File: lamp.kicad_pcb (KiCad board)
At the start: 2 copper layers, 74.7 x 38.6 mm, 25 parts, among them J1 Screw_Terminal_01x02, J2 Screw_Terminal_01x02, J3 Conn_01x04_Pin, K1 G3MB202PDC12, Q1 BC547, U1 ESP-12E, U3 AMS1117-3.3

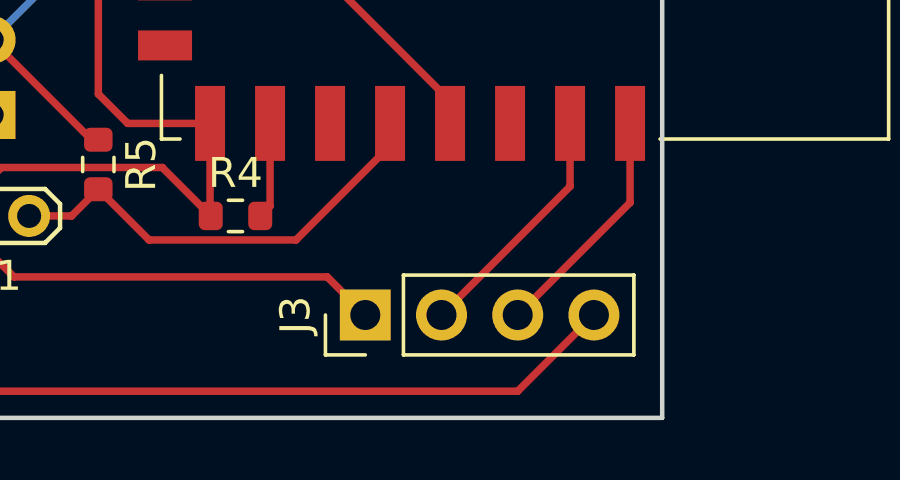
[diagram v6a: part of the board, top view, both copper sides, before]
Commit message: fix jumper side
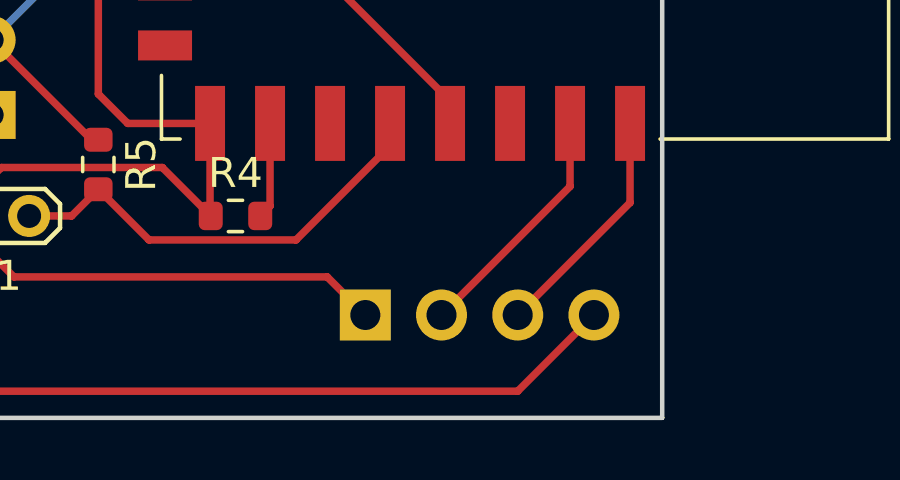
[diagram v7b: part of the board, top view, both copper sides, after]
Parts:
- J3: moved to B.Cu
- turned J3 to -90 degrees
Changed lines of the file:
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@@
-    )
-  )
-  (footprint "Connector_PinHeader_2.54mm:PinHeader_1x04_P2.54mm_Vertical" (layer "F.Cu")
-    (at 179.08 133.35 90)
-    (descr "Through hole straight pin header, 1x04, 2.54mm pitch, single row")
-    (tags "Through hole pin header THT 1x04 2.54mm single row")
-    (property "Sheetfile" "lamp.kicad_sch")
-    (property "Sheetname" "")
-    (property "ki_description" "Generic connector, single row, 01x04, script generated")
-    (property "ki_keywords" "connector")
-    (attr through_hole)
-    (fp_text reference "J3" (at 0 -2.33 90) (layer "F.SilkS")
-        (effects (font (size 1 1) (thickness 0.15)))
-    )
-    (fp_text value "Conn_01x04_Pin" (at 0 9.95 90) (layer "F.Fab") hide
-        (effects (font (size 1 1) (thickness 0.15)))
-    )
-    (fp_text user "${REFERENCE}" (at 0 3.81) (layer "F.Fab")
-        (effects (font (size 1 1) (thickness 0.15)))
-    )
-    (fp_line (start -1.33 -1.33) (end 0 -1.33)
-      (stroke (width 0.12) (type solid)) (layer "F.SilkS"))
-    (fp_line (start -1.33 0) (end -1.33 -1.33)
-      (stroke (width 0.12) (type solid)) (layer "F.SilkS"))
-    (fp_line (start -1.33 1.27) (end -1.33 8.95)
-      (stroke (width 0.12) (type solid)) (layer "F.SilkS"))
-    (fp_line (start -1.33 1.27) (end 1.33 1.27)
-      (stroke (width 0.12) (type solid)) (layer "F.SilkS"))
-    (fp_line (start -1.33 8.95) (end 1.33 8.95)
-      (stroke (width 0.12) (type solid)) (layer "F.SilkS"))
-    (fp_line (start 1.33 1.27) (end 1.33 8.95)
-      (stroke (width 0.12) (type solid)) (layer "F.SilkS"))
-    (fp_line (start -1.8 -1.8) (end -1.8 9.4)
-      (stroke (width 0.05) (type solid)) (layer "F.CrtYd"))
-    (fp_line (start -1.8 9.4) (end 1.8 9.4)
-      (stroke (width 0.05) (type solid)) (layer "F.CrtYd"))
-    (fp_line (start 1.8 -1.8) (end -1.8 -1.8)
-      (stroke (width 0.05) (type solid)) (layer "F.CrtYd"))
-    (fp_line (start 1.8 9.4) (end 1.8 -1.8)
-      (stroke (width 0.05) (type solid)) (layer "F.CrtYd"))
-    (fp_line (start -1.27 -0.635) (end -0.635 -1.27)
-      (stroke (width 0.1) (type solid)) (layer "F.Fab"))
-    (fp_line (start -1.27 8.89) (end -1.27 -0.635)
-      (stroke (width 0.1) (type solid)) (layer "F.Fab"))
-    (fp_line (start -0.635 -1.27) (end 1.27 -1.27)
-      (stroke (width 0.1) (type solid)) (layer "F.Fab"))
-    (fp_line (start 1.27 -1.27) (end 1.27 8.89)
-      (stroke (width 0.1) (type solid)) (layer "F.Fab"))
-    (fp_line (start 1.27 8.89) (end -1.27 8.89)
-      (stroke (width 0.1) (type solid)) (layer "F.Fab"))
-    (pad "1" thru_hole rect (at 0 0 90) (size 1.7 1.7) (drill 1) (layers "*.Cu" "*.Mask")
-      (net 1 "GND") (pinfunction "Pin_1") (pintype "passive"))
-    (pad "2" thru_hole oval (at 0 2.54 90) (size 1.7 1.7) (drill 1) (layers "*.Cu" "*.Mask")
-      (net 29 "Net-(J3-Pin_2)") (pinfunction "Pin_2") (pintype "passive"))
-    (pad "3" thru_hole oval (at 0 5.08 90) (size 1.7 1.7) (drill 1) (layers "*.Cu" "*.Mask")
-      (net 30 "Net-(J3-Pin_3)") (pinfunction "Pin_3") (pintype "passive"))
-    (pad "4" thru_hole oval (at 0 7.62 90) (size 1.7 1.7) (drill 1) (layers "*.Cu" "*.Mask")
-      (net 31 "Net-(J3-Pin_4)") (pinfunction "Pin_4") (pintype "passive"))
-    (model "${KICAD6_3DMODEL_DIR}/Connector_PinHeader_2.54mm.3dshapes/PinHeader_1x04_P2.54mm_Vertical.wrl"
-      (offset (xyz 0 0 0))
-      (scale (xyz 1 1 1))
-      (rotate (xyz 0 0 0))
     )
   )
@@
       (net 3 "Net-(D1-K)") (pinfunction "-") (pintype "power_in"))
   )
+  (footprint "Connector_PinHeader_2.54mm:PinHeader_1x04_P2.54mm_Vertical" (layer "B.Cu")
+    (at 179.08 133.35 -90)
+    (descr "Through hole straight pin header, 1x04, 2.54mm pitch, single row")
+    (tags "Through hole pin header THT 1x04 2.54mm single row")
+    (property "Sheetfile" "lamp.kicad_sch")
+    (property "Sheetname" "")
+    (property "ki_description" "Generic connector, single row, 01x04, script generated")
+    (property "ki_keywords" "connector")
+    (attr through_hole)
+    (fp_text reference "J3" (at 0 2.33 90) (layer "B.SilkS")
+        (effects (font (size 1 1) (thickness 0.15)) (justify mirror))
+    )
+    (fp_text value "Conn_01x04_Pin" (at 0 -9.95 90) (layer "B.Fab") hide
+        (effects (font (size 1 1) (thickness 0.15)) (justify mirror))
+    )
+    (fp_text user "${REFERENCE}" (at 0 -3.81) (layer "B.Fab")
+        (effects (font (size 1 1) (thickness 0.15)) (justify mirror))
+    )
+    (fp_line (start -1.33 -8.95) (end 1.33 -8.95)
+      (stroke (width 0.12) (type solid)) (layer "B.SilkS"))
+    (fp_line (start -1.33 -1.27) (end -1.33 -8.95)
+      (stroke (width 0.12) (type solid)) (layer "B.SilkS"))
+    (fp_line (start -1.33 -1.27) (end 1.33 -1.27)
+      (stroke (width 0.12) (type solid)) (layer "B.SilkS"))
+    (fp_line (start -1.33 0) (end -1.33 1.33)
+      (stroke (width 0.12) (type solid)) (layer "B.SilkS"))
+    (fp_line (start -1.33 1.33) (end 0 1.33)
+      (stroke (width 0.12) (type solid)) (layer "B.SilkS"))
+    (fp_line (start 1.33 -1.27) (end 1.33 -8.95)
+      (stroke (width 0.12) (type solid)) (layer "B.SilkS"))
+    (fp_line (start -1.8 -9.4) (end 1.8 -9.4)
+      (stroke (width 0.05) (type solid)) (layer "B.CrtYd"))
+    (fp_line (start -1.8 1.8) (end -1.8 -9.4)
+      (stroke (width 0.05) (type solid)) (layer "B.CrtYd"))
+    (fp_line (start 1.8 -9.4) (end 1.8 1.8)
+      (stroke (width 0.05) (type solid)) (layer "B.CrtYd"))
+    (fp_line (start 1.8 1.8) (end -1.8 1.8)
+      (stroke (width 0.05) (type solid)) (layer "B.CrtYd"))
+    (fp_line (start -1.27 -8.89) (end -1.27 0.635)
+      (stroke (width 0.1) (type solid)) (layer "B.Fab"))
+    (fp_line (start -1.27 0.635) (end -0.635 1.27)
+      (stroke (width 0.1) (type solid)) (layer "B.Fab"))
+    (fp_line (start -0.635 1.27) (end 1.27 1.27)
+      (stroke (width 0.1) (type solid)) (layer "B.Fab"))
+    (fp_line (start 1.27 -8.89) (end -1.27 -8.89)
+      (stroke (width 0.1) (type solid)) (layer "B.Fab"))
+    (fp_line (start 1.27 1.27) (end 1.27 -8.89)
+      (stroke (width 0.1) (type solid)) (layer "B.Fab"))
+    (pad "1" thru_hole rect (at 0 0 270) (size 1.7 1.7) (drill 1) (layers "*.Cu" "*.Mask")
+      (net 1 "GND") (pinfunction "Pin_1") (pintype "passive"))
+    (pad "2" thru_hole oval (at 0 -2.54 270) (size 1.7 1.7) (drill 1) (layers "*.Cu" "*.Mask")
+      (net 29 "Net-(J3-Pin_2)") (pinfunction "Pin_2") (pintype "passive"))
+    (pad "3" thru_hole oval (at 0 -5.08 270) (size 1.7 1.7) (drill 1) (layers "*.Cu" "*.Mask")
+      (net 30 "Net-(J3-Pin_3)") (pinfunction "Pin_3") (pintype "passive"))
+    (pad "4" thru_hole oval (at 0 -7.62 270) (size 1.7 1.7) (drill 1) (layers "*.Cu" "*.Mask")
+      (net 31 "Net-(J3-Pin_4)") (pinfunction "Pin_4") (pintype "passive"))
+    (model "${KICAD6_3DMODEL_DIR}/Connector_PinHeader_2.54mm.3dshapes/PinHeader_1x04_P2.54mm_Vertical.wrl"
+      (offset (xyz 0 0 0))
+      (scale (xyz 1 1 1))
+      (rotate (xyz 0 0 0))
+    )
+  )
   (footprint "Capacitor_THT:CP_Radial_D5.0mm_P2.50mm" (layer "B.Cu")
